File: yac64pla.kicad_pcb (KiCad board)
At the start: 2 copper layers, 18.8 x 37.3 mm, 4 parts, among them U1 GAL20V8_L, U2 GAL20V8_R, U3 C64_PLA

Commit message: Rename left/right to top/bottom
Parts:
- U1: value GAL20V8_L -> PLD_TOP
- U2: value GAL20V8_R -> PLD_BOTTOM
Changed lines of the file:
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@@
       (effects (font (size 1 1) (thickness 0.15)))
     )
-    (fp_text value "GAL20V8_R" (at 0 7.285 90) (layer "F.Fab")
+    (fp_text value "PLD_BOTTOM" (at 0 7.285 90) (layer "F.Fab")
       (effects (font (size 1 1) (thickness 0.15)))
     )
@@
       (effects (font (size 1 1) (thickness 0.15)))
     )
-    (fp_text value "GAL20V8_L" (at 0 7.285 90) (layer "F.Fab")
-      (effects (font (size 1 1) (thickness 0.15)))
-    )
+    (fp_text value "PLD_TOP" (at 0 7.285 90) (layer "F.Fab")
+      (effects (font (size 1 1) (thickness 0.15)))
+    )

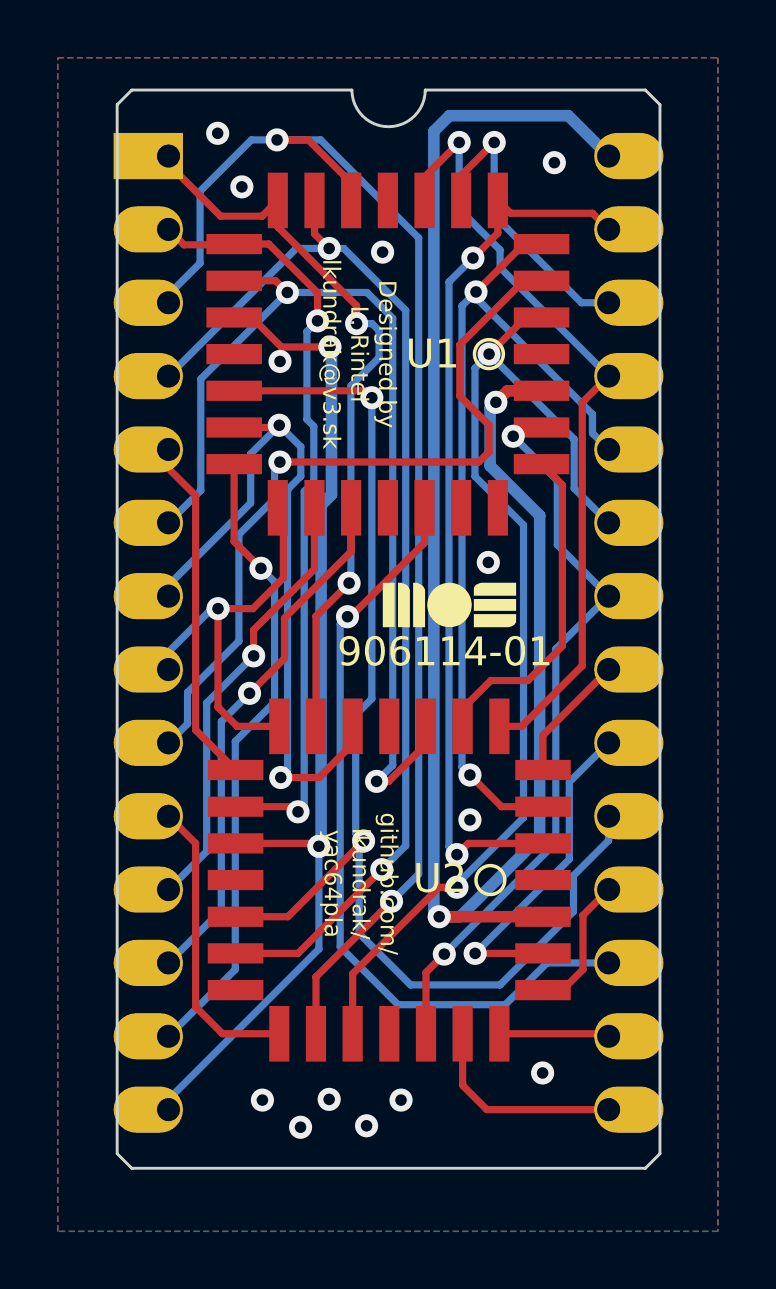
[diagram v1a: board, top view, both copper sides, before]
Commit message: Slight layout improvements
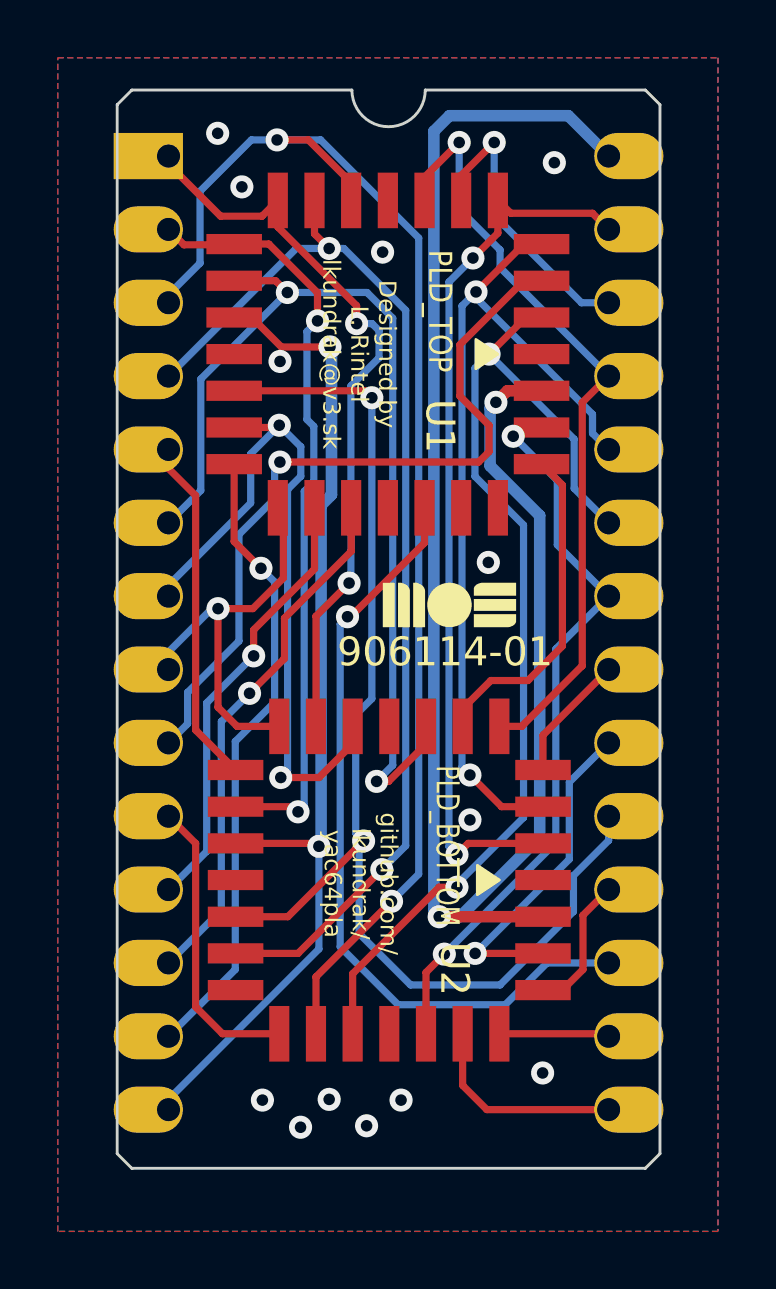
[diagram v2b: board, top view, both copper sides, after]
